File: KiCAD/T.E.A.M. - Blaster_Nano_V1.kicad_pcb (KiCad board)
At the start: 2 copper layers, 47 parts, among them J1 USB_C_Receptacle_USB2.0_14P, J2 Conn_01x02, J3 Conn_01x02, J4 Conn_01x02, J5 Conn_01x02, J6 Conn_02x03_Counter_Clockwise, Q1 FS8205A, U1 TP4056-42-ESOP8, U2 DW01A, U3 MT3608, U4 ATMEGA328P-AU, U5 CH340G, U6 DFR0299, Y1 Crystal, Y2 Crystal

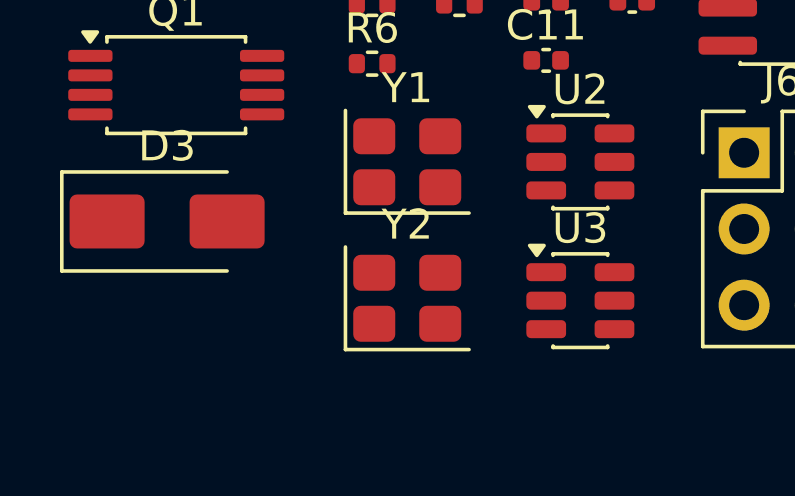
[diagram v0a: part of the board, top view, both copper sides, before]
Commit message: Add Crystal_GND31 symbol and connect crystal shield to GND
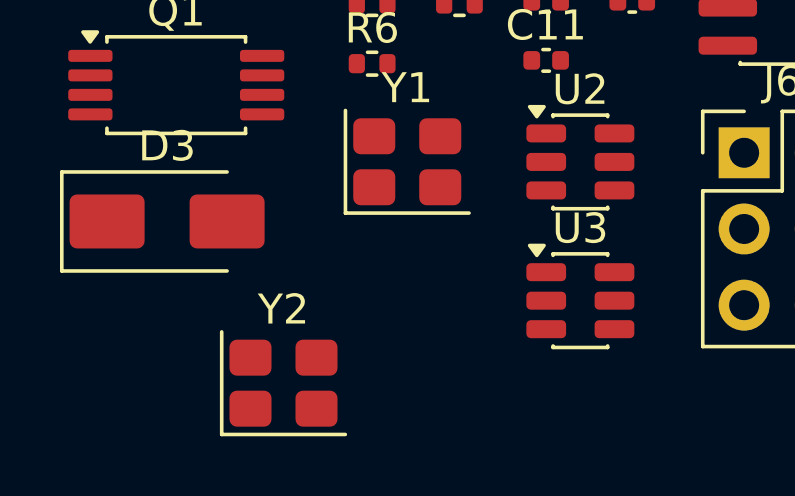
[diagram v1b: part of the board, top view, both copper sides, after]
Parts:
- Y1, Y2: value Crystal -> Crystal_GND34
- moved Y2 5.00 mm to (238.6, 156.0)
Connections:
- Y1 pad 3: (no net) -> GND
- Y1 pad 4: (no net) -> GND
- Y2 pad 3: (no net) -> GND
- Y2 pad 4: (no net) -> GND
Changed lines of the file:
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@@
 			)
 		)
-		(property "Value" "Crystal"
+		(property "Value" "Crystal_GND34"
 			(at 0 2.45 0)
 			(layer "F.Fab")
@@
 			)
 		)
-		(property "Description" "Crystal"
+		(property "Description" "Four pin crystal, GND on pins 2 and 3"
 			(at 0 0 0)
 			(layer "F.Fab")
@@
 			(unit
 				(name "A")
-				(pins "1" "2")
+				(pins "1" "3" "4" "2")
 			)
 		)
@@
 			(roundrect_rratio 0.208333)
 			(net "Net-(U4-PB7)")
-			(pinfunction "2_2")
+			(pinfunction "4_2")
 			(pintype "passive")
 		)
@@
 			(layers "F.Cu" "F.Mask" "F.Paste")
 			(roundrect_rratio 0.208333)
+			(net "GND")
+			(pinfunction "G_3")
+			(pintype "passive")
 		)
 		(pad "4" smd roundrect
@@
 			(layers "F.Cu" "F.Mask" "F.Paste")
 			(roundrect_rratio 0.208333)
+			(net "GND")
+			(pinfunction "G_4")
+			(pintype "passive")
 		)
 		(embedded_fonts no)
@@
 	(footprint "Crystal:Crystal_SMD_3225-4Pin_3.2x2.5mm"
 		(layer "F.Cu")
-		(at 242.715 153.165)
+		(at 238.59 155.995)
 		(descr "SMD3225/4, Crystal, 3.2x2.5mm package, SMD, http://www.txccrystal.com/images/pdf/7m-accuracy.pdf")
 		(property "Reference" "Y2"
@@
 			)
 		)
-		(property "Value" "Crystal"
+		(property "Value" "Crystal_GND34"
 			(at 0 2.45 0)
 			(layer "F.Fab")
@@
 			)
 		)
-		(property "Description" "Crystal"
+		(property "Description" "Four pin crystal, GND on pins 2 and 3"
 			(at 0 0 0)
 			(layer "F.Fab")
@@
 			(unit
 				(name "A")
-				(pins "1" "2")
+				(pins "1" "3" "4" "2")
 			)
 		)
@@
 			(roundrect_rratio 0.208333)
 			(net "Net-(U5-XI)")
-			(pinfunction "2_2")
+			(pinfunction "4_2")
 			(pintype "passive")
 		)
@@
 			(layers "F.Cu" "F.Mask" "F.Paste")
 			(roundrect_rratio 0.208333)
+			(net "GND")
+			(pinfunction "G_3")
+			(pintype "passive")
 		)
 		(pad "4" smd roundrect
@@
 			(layers "F.Cu" "F.Mask" "F.Paste")
 			(roundrect_rratio 0.208333)
+			(net "GND")
+			(pinfunction "G_4")
+			(pintype "passive")
 		)
 		(embedded_fonts no)

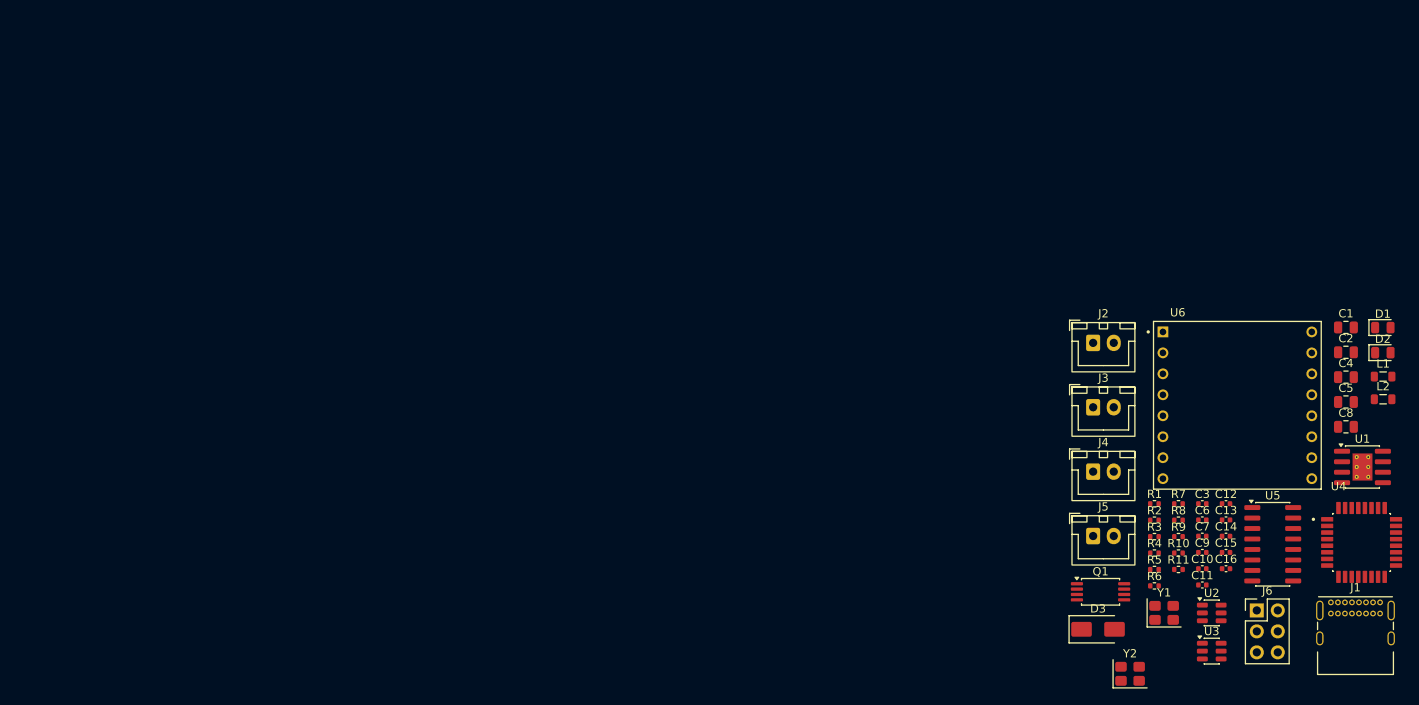
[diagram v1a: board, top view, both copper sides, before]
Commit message: Add 3D models for U1, U4, U6
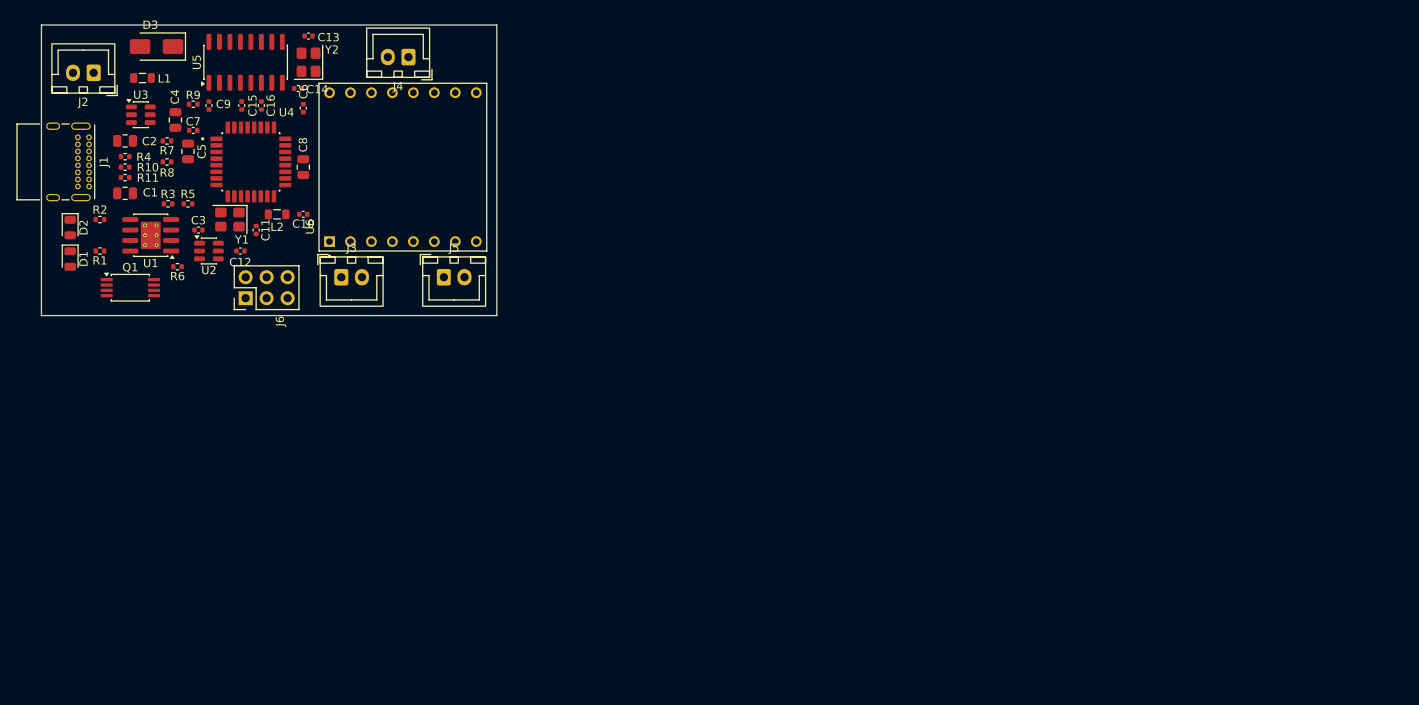
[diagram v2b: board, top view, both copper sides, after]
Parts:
- D1: value LED -> LED rot
- D2: value LED -> LED blau
- J2: value Conn_01x02 -> AKKU
- J3: value Conn_01x02 -> LED
- J4: value Conn_01x02 -> Taster
- J5: value Conn_01x02 -> Speaker
- moved J1 160.7 mm to (112.5, 91.0), turned to -90 degrees
- moved D2 159.7 mm to (110.2, 101.9), turned to -90 degrees
- moved D1 159.2 mm to (110.2, 105.7), turned to -90 degrees
- moved L1 154.6 mm to (119.0, 83.8), turned to 180 degrees
- moved C2 150.1 mm to (116.8, 91.4)
- moved U1 149.5 mm to (120.0, 102.9), turned to 180 degrees
- moved C1 148.8 mm to (116.8, 97.8)
- moved C4 145.2 mm to (122.9, 88.9), turned to 90 degrees
- moved U3 145.1 mm to (118.7, 88.3)
- moved C5 143.5 mm to (124.5, 92.7), turned to -90 degrees
- moved U4 142.2 mm to (132.1, 94.0)
- moved U5 137.4 mm to (131.4, 81.9), turned to 90 degrees
- moved R11 136.2 mm to (116.8, 95.9)
- moved R10 135.9 mm to (116.8, 94.6)
- moved L2 135.9 mm to (135.3, 100.3), turned to 180 degrees
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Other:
- board outline added: 55.2 x 35.2 mm
